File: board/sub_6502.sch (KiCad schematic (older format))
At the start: 18 parts, among them Q1201 Q_NPN_BEC, U1201 74HCT245, U1202 74HCT245, U1203 74HCT245, U1204 6502, U1205 74HCT245

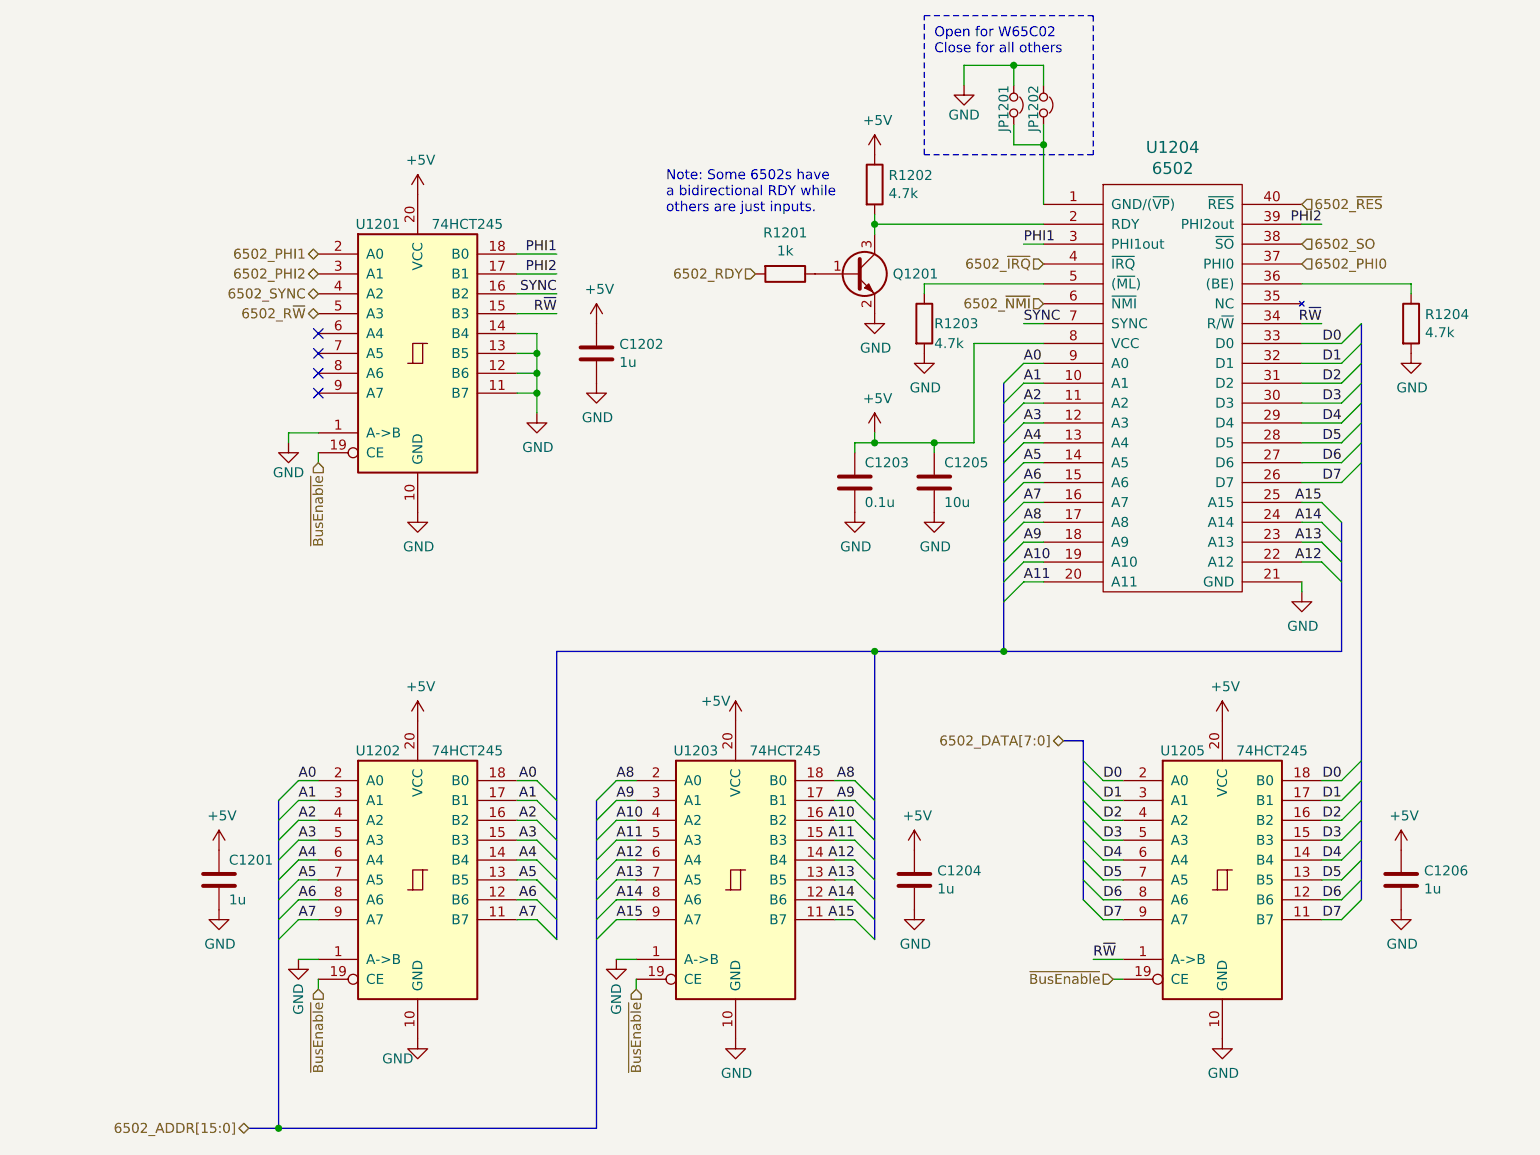
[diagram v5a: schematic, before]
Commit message: Bus signal connectivity rebuilt
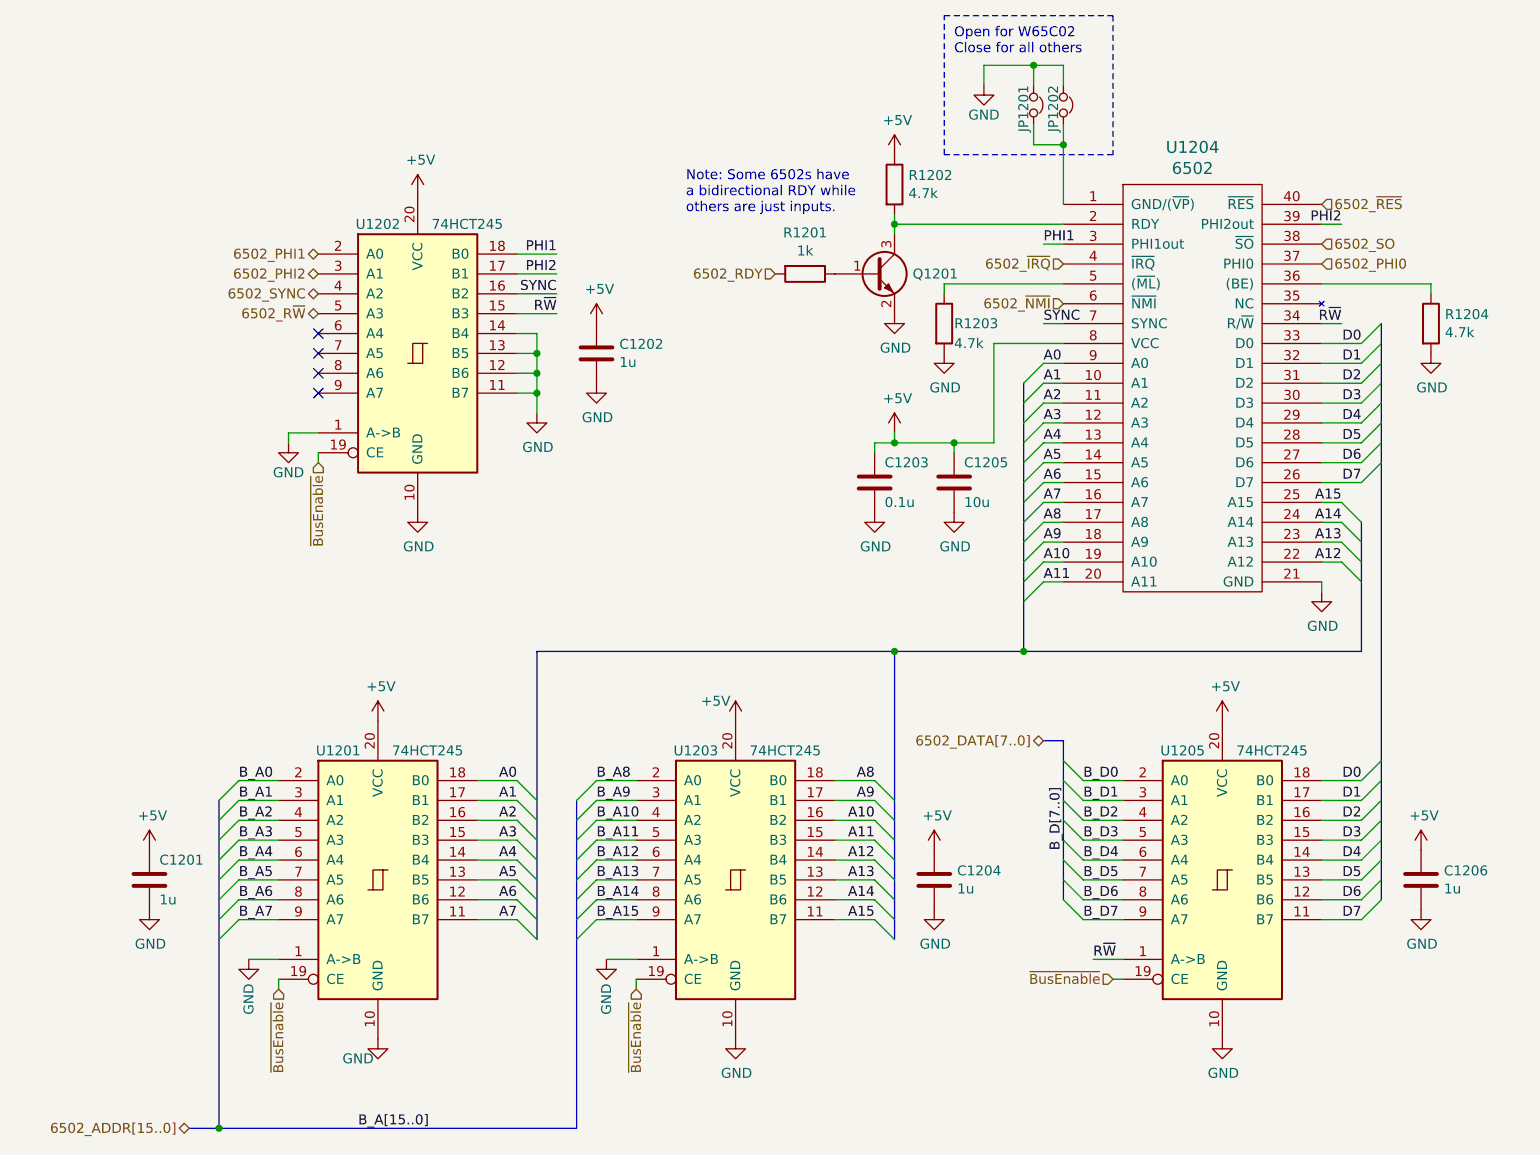
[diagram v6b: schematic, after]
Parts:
- renumbered U1202 to U1201, U1201 to U1202
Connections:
- net A0: no longer U1201.2 (A0)
- net A1: no longer U1201.3 (A1)
- net A10: no longer U1203.4 (A2)
- net A11: no longer U1203.5 (A3)
- net A12: no longer U1203.6 (A4)
- net A13: no longer U1203.7 (A5)
- net A14: no longer U1203.8 (A6)
- net A15: no longer U1203.9 (A7)
- net A2: no longer U1201.4 (A2)
- net A3: no longer U1201.5 (A3)
- net A4: no longer U1201.6 (A4)
- net A5: no longer U1201.7 (A5)
- net A6: no longer U1201.8 (A6)
- net A7: no longer U1201.9 (A7)
- net A8: no longer U1203.2 (A0)
- net A9: no longer U1203.3 (A1)
- net D0: no longer U1205.2 (A0)
- net D1: no longer U1205.3 (A1)
- net D2: no longer U1205.4 (A2)
- net D3: no longer U1205.5 (A3)
- net D4: no longer U1205.6 (A4)
- net D5: no longer U1205.7 (A5)
- net D6: no longer U1205.8 (A6)
- net D7: no longer U1205.9 (A7)
- new net B_A0: U1201.2 (A0)
- new net B_A1: U1201.3 (A1)
- new net B_A10: U1203.4 (A2)
- new net B_A11: U1203.5 (A3)
- new net B_A12: U1203.6 (A4)
- new net B_A13: U1203.7 (A5)
- new net B_A14: U1203.8 (A6)
- new net B_A15: U1203.9 (A7)
- new net B_A2: U1201.4 (A2)
- new net B_A3: U1201.5 (A3)
- new net B_A4: U1201.6 (A4)
- new net B_A5: U1201.7 (A5)
- new net B_A6: U1201.8 (A6)
- new net B_A7: U1201.9 (A7)
- new net B_A8: U1203.2 (A0)
- new net B_A9: U1203.3 (A1)
- new net B_D0: U1205.2 (A0)
- new net B_D1: U1205.3 (A1)
- new net B_D2: U1205.4 (A2)
- new net B_D3: U1205.5 (A3)
- new net B_D4: U1205.6 (A4)
- new net B_D5: U1205.7 (A5)
- new net B_D6: U1205.8 (A6)
- new net B_D7: U1205.9 (A7)
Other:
- moved on the sheet: C1201, C1203, C1204, C1205, C1206, JP1201, JP1202, Q1201, R1201, R1202, R1203, R1204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

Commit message: gpio done
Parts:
- U1201, U1202, U1203, U1205: symbol Logic_74xx:74HC245 -> 74xx:74HC245
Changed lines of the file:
@@
 $EndComp
 $Comp
-L Logic_74xx:74HC245 U1205
+L 74xx:74HC245 U1205
 U 1 1 5AA3AAEF
 P 9350 5000
@@
 	8800 5500 8850 5500
 $Comp
-L Logic_74xx:74HC245 U1201
+L 74xx:74HC245 U1201
 U 1 1 5AA5D878
 P 5100 5000
@@
 $EndComp
 $Comp
-L Logic_74xx:74HC245 U1203
+L 74xx:74HC245 U1203
 U 1 1 5AA5D9D4
 P 6900 5000
@@
 Connection ~ 4300 6250
 $Comp
-L Logic_74xx:74HC245 U1202
+L 74xx:74HC245 U1202
 U 1 1 5AB27A32
 P 5300 2350

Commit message: Schematics mostly complete
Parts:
- removed R1203: 4.7k, symbol Device:R
- renumbered C1202 to C1201, C1203 to C1202, C1205 to C1203, C1201 to C1204, C1204 to C1205, R1202 to R1201, R1204 to R1202, R1201 to R1203, U1202 to U1201, U1204 to U1202, U1201 to U1203, U1203 to U1204
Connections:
- net +5V: now also R1202.1
- net GND: no longer R1202.2
- net at U1202.36 ((BE)): now also R1202.2; no longer R1202.1
- no-connect marks 4 -> 5
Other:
- moved on the sheet: R1202
